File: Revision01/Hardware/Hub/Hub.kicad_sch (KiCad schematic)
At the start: 27 parts, among them J20 Conn_01x04, J3 Conn_01x04, J4 Conn_01x05, J5 Conn_01x05, SW1 ON/OFF_SW_SPST_LED, U1 NUCLEO-L476RG, U2 LMR51603XFDBVR

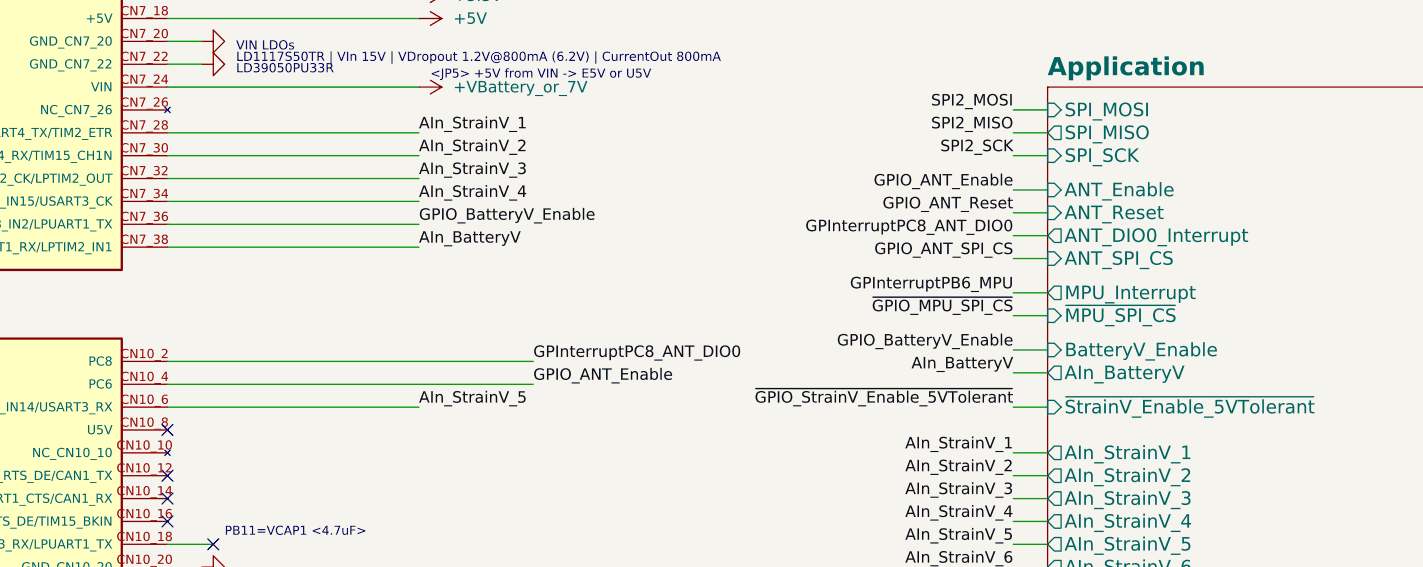
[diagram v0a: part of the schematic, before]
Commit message: . Changed battery measurement switch to 1/5 1/2 mA, uses the same components as the regular analog in chain . Added simulation for battery measurement "switch" . Checked DRC & ERC
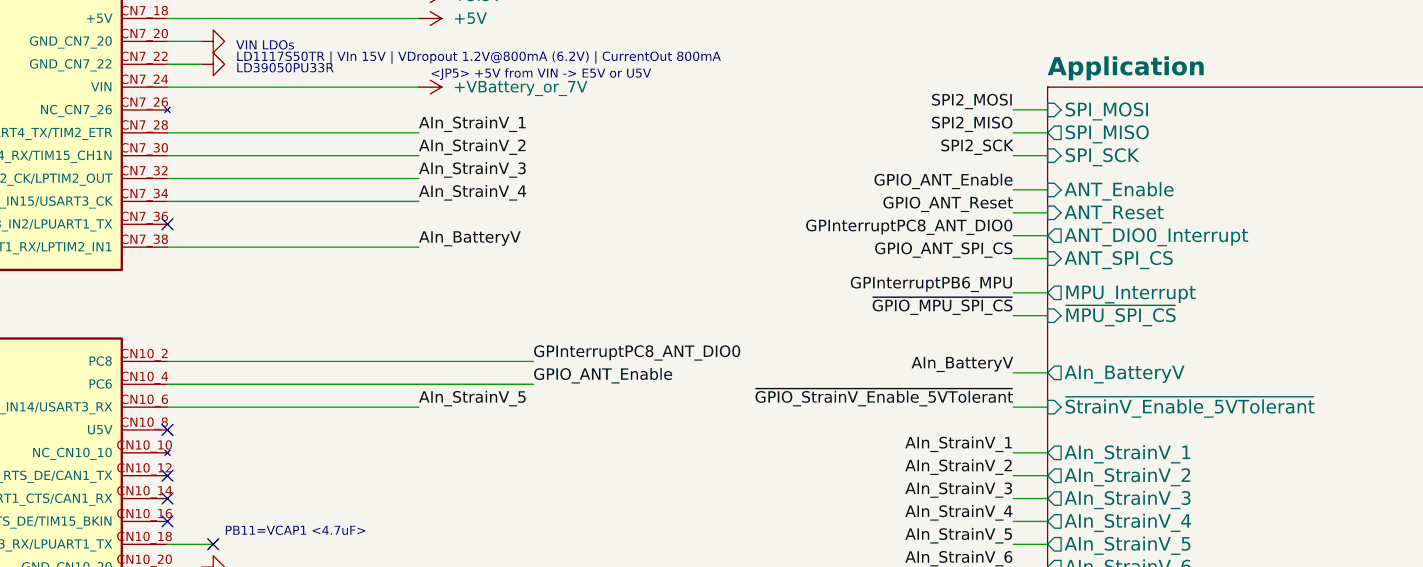
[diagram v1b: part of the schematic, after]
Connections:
- net GPIO_BatteryV_Enable: no longer names the net of U1.CN7_36 (PC1/ADC123_IN2/LPUART1_TX)
- no-connect marks 41 -> 42
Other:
- sheet Application ports: added none; removed BatteryV_Enable
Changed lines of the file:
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@@
 	)
 	(no_connect
+		(at 213.36 171.45)
+	)
+	(no_connect
 		(at 213.36 194.31)
 	)
@@
 	(wire
 		(pts
-			(xy 307.34 185.42) (xy 311.15 185.42)
-		)
-		(stroke
-			(width 0)
-			(type default)
-		)
-	)
-	(wire
-		(pts
 			(xy 49.53 71.12) (xy 50.8 71.12)
 		)
@@
 	(wire
 		(pts
-			(xy 241.3 171.45) (xy 213.36 171.45)
-		)
-		(stroke
-			(width 0)
-			(type default)
-		)
-	)
-	(wire
-		(pts
 			(xy 223.52 60.96) (xy 223.52 63.5)
 		)
@@
 		)
 	)
-	(label "GPIO_BatteryV_Enable"
-		(at 241.3 171.45 0)
-		(effects
-			(font
-				(size 1.27 1.27)
-			)
-			(justify left bottom)
-		)
-	)
 	(label "GPInterruptPB6_MPU"
 		(at 307.34 179.07 180)
@@
 		)
 	)
-	(label "GPIO_BatteryV_Enable"
-		(at 307.34 185.42 180)
-		(effects
-			(font
-				(size 1.27 1.27)
-			)
-			(justify right bottom)
-		)
-	)
 	(label "SPI2_MOSI"
 		(at 241.3 217.17 0)
@@
 			(effects
 				(font
-					(size 1.4986 1.4986)
-				)
-				(justify left)
-			)
-		)
-		(pin "BatteryV_Enable" input
-			(at 311.15 185.42 180)
-			(effects
-				(font

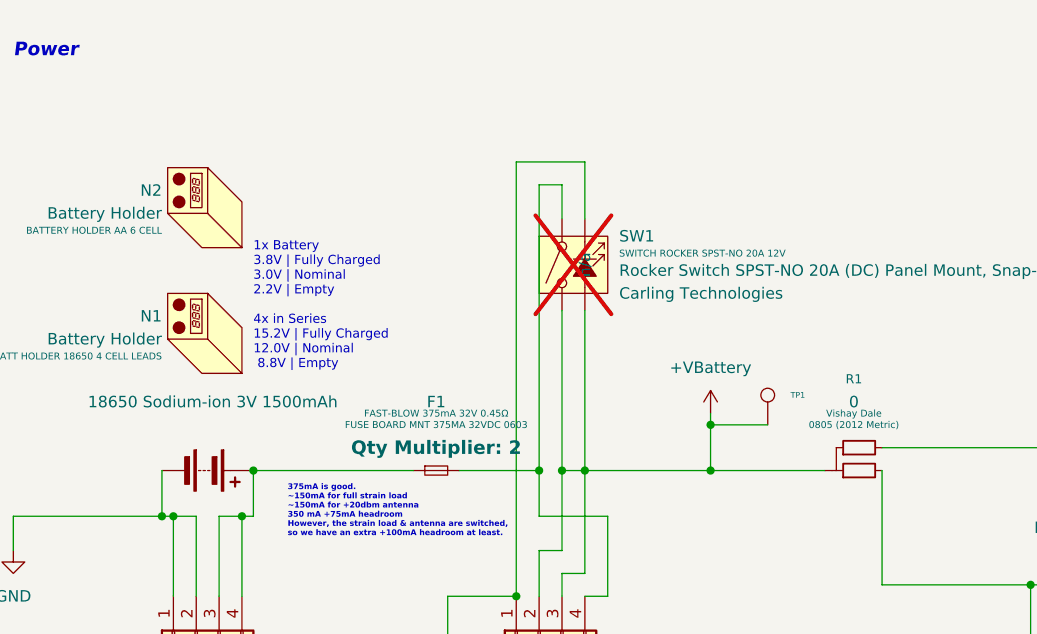
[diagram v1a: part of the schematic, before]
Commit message: small visual changes - put X on bypass 0 ohm resistor - do not populate on extra-battery type
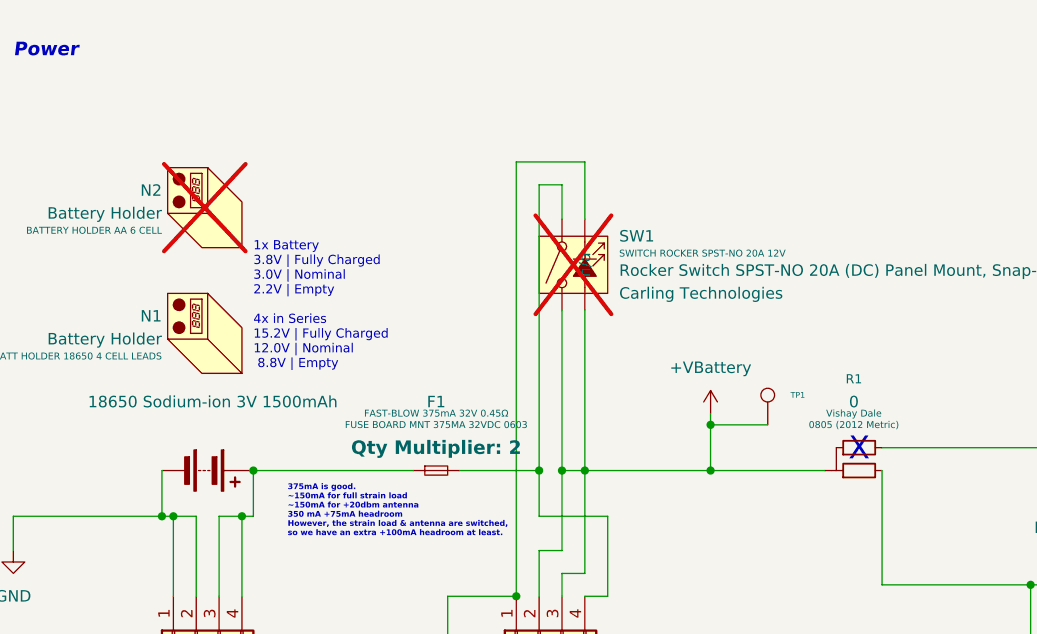
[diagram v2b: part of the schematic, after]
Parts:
- N2: now not fitted
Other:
- note added: "X"
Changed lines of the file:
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@@
 		)
 	)
+	(text "X"
+		(exclude_from_sim no)
+		(at 118.11 63.754 0)
+		(effects
+			(font
+				(size 2.54 2.54)
+				(color 255 0 0 1)
+			)
+		)
+	)
 	(text "PC13 | PC13 <SB17> B1, Blue PB"
 		(exclude_from_sim no)
@@
 		(in_bom yes)
 		(on_board no)
-		(dnp no)
+		(dnp yes)
 		(fields_autoplaced yes)
 		(property "Reference" "N2"
